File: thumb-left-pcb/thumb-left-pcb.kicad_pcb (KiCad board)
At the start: 2 copper layers, 77 x 88 mm, 31 parts, among them J1 Conn_01x10

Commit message: sync left schematic with pcb
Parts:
- renumbered C66 to C25, C86 to C35, C65 to C36, C75 to C46, C96 to C55, C85 to C56, D66 to D25, D86 to D35, D65 to D36, D75 to D46, D96 to D55, D85 to D56, LED66 to LED25, LED86 to LED35, LED65 to LED36, LED75 to LED46, LED96 to LED55, LED85 to LED56, MX66 to MX25, MX86 to MX35, MX65 to MX36, MX75 to MX46, MX96 to MX55, MX85 to MX56
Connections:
- D25 pad 1: /ROW_6 -> /ROW_2
- D35 pad 1: /ROW_8 -> /ROW_3
- D36 pad 1: /ROW_6 -> /ROW_3
- D46 pad 1: /ROW_7 -> /ROW_4
- D55 pad 1: /ROW_9 -> /COL_R6
- D56 pad 1: /ROW_8 -> /COL_R6
- J1 pad 1: /DIN -> /ROW_4
- J1 pad 2: /DOUT -> /ROW_2
- J1 pad 3: /ROW_6 -> /COL_R6
- J1 pad 4: /ROW_7 -> /COL_6
- J1 pad 5: /ROW_8 -> /COL_5
- J1 pad 6: /ROW_9 -> /DIN
- J1 pad 7: /COL_R6 -> /DOUT
- J1 pad 8: /COL_R5 -> /ROW_3
- MX25 pad 2: /COL_R6 -> /COL_R5
- MX35 pad 2: /COL_R6 -> /COL_R5
- MX36 pad 2: /COL_R5 -> /COL_R6
- MX46 pad 2: /COL_R5 -> /COL_R6
- MX55 pad 2: /COL_R6 -> /COL_R5
- MX56 pad 2: /COL_R5 -> /COL_R6

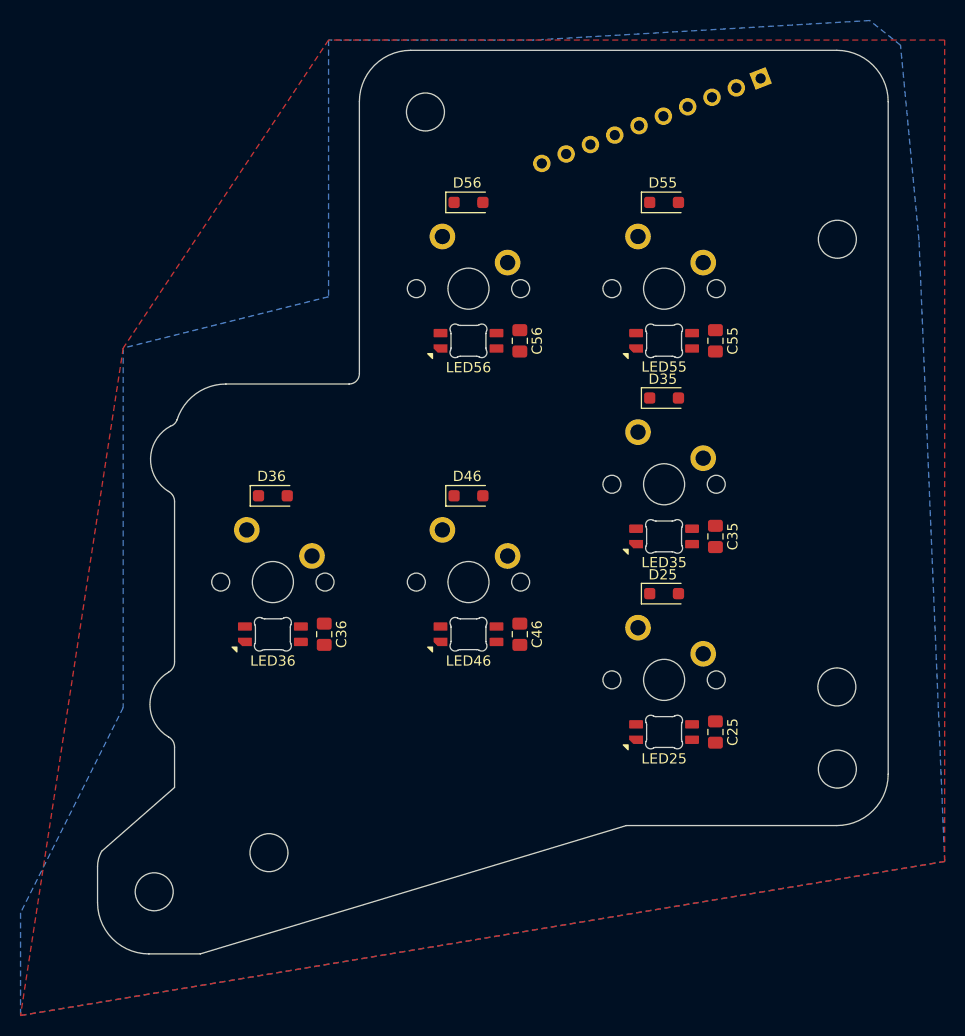
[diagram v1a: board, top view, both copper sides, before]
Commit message: move components to correct side
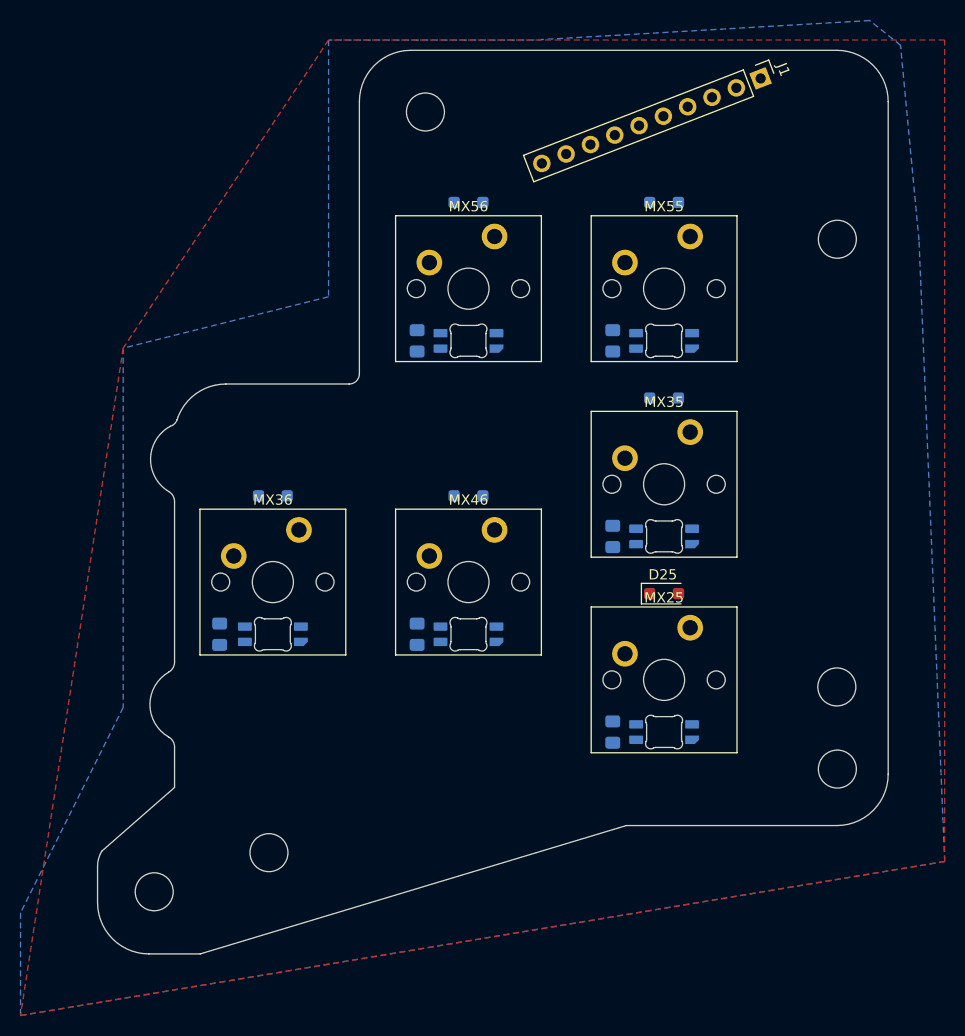
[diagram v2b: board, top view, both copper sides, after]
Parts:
- C25, C35, C36, C46, C55, C56, D35, D36, D46, D55, D56, LED25, LED35, LED36, LED46, LED55, LED56: moved to B.Cu
- J1, MX25, MX35, MX36, MX46, MX55, MX56: moved to F.Cu
- moved C36 10.2 mm to (179.4, 82.9)
- moved C25 10.0 mm to (217.7, 92.4)
- moved C35 10.0 mm to (217.7, 73.3)
- moved C46 10.0 mm to (198.6, 82.9)
- moved C55 10.0 mm to (217.7, 54.3)
- moved C56 10.0 mm to (198.6, 54.3)
- turned D35 to 180 degrees
- turned D36 to 180 degrees
- turned D46 to 180 degrees
- turned D55 to 180 degrees
- turned D56 to 180 degrees
- turned J1 to -68.769 degrees
- turned LED25 to 180 degrees
- turned LED35 to 180 degrees
- turned LED36 to 180 degrees
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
